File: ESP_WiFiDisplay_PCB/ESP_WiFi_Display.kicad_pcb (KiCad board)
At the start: 2 copper layers, 50 x 100 mm, 30 parts, among them CON1 BARREL_JACK, P1 SERIAL_HC12, P10 POWER, P2 USB, P3 NODEMCU_1, P4 NODEMCU_2, P5 LOCAL 5V?, P6 WS2812 LED, P7 PCB, P8 LOGO1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

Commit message: PCB changes
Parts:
- removed CON1: BARREL_JACK, REInnovationFootprint:DC_Power_2_1
- removed R2: 330, REInnovationFootprint:TH_Resistor_1
- removed R3, R4: 10k, REInnovationFootprint:TH_Resistor_1
- removed SW2: SWDOWN, REInnovationFootprint:SW_PUSH_SMALL_lg_pad
- removed SW3: ON/OFF, REInnovationFootprint:SW_SPDT_R_Angle_ALIEX
- removed U3: 74LVC1G17, REInnovationFootprint:SM_SOT-23-5
- added C3: 100n, matts_components:C1_wide_lg_pad, F.Cu at (112.4, 47.0)
- added C4: 100n, matts_components:C1_wide_lg_pad, F.Cu at (121.3, 47.0)
- added C5: 100n, matts_components:C1_wide_lg_pad, F.Cu at (130.2, 47.0)
- added D6: WS2812, LEDs:LED_WS2812B-PLCC4, F.Cu at (122.6, 41.9)
- added D7: WS2812, LEDs:LED_WS2812B-PLCC4, F.Cu at (131.4, 41.9)
- added ENC1: Encoder_1, matts_components:Encoder, F.Cu at (113.7, 112.4)
- C1, C2: value 10u -> 100n; footprint REInnovationFootprint:C_1V7_TH -> matts_components:C1_wide_lg_pad
- D1: value WS2811_EpiStar_8mm -> D_Schottky; footprint REInnovationFootprint:TH_WS2811_LED_8mm -> REInnovationFootprint:TH_Diode_1
- D2: value A -> B
- D3: value B -> WS2812; footprint REInnovationFootprint:TH_LED-5MM_larg_pad -> LEDs:LED_WS2812B-PLCC4
- D4, D5: value D_Schottky -> WS2812; footprint REInnovationFootprint:TH_Diode_1 -> LEDs:LED_WS2812B-PLCC4
- P1: value SERIAL_HC12 -> USB_Micro; footprint REInnovationFootprint:TH_SIL_5_1mm -> REInnovationFootprint:USB_Micro-B_MOLEX_47642-0001
- P10: value POWER -> 5V_EXT; footprint REInnovationFootprint:SIL-2_screw_terminal -> REInnovationFootprint:TH_CONN_2W
- P5: value LOCAL 5V? -> PCB; footprint matts_components:SIL-2_solder_connect -> REInnovationFootprint:PCB_50x100mm_RJWIFI
- P6: value WS2812 LED -> LOGO1; footprint matts_components:SIL-4_screw_terminals -> CuriousElectric3:CEC_Globe_10mm_FCU
- P7: value PCB -> LOGO2; footprint REInnovationFootprint:PCB_50x100mm_RJWIFI -> CuriousElectric3:TCEC_Words_13mm
- P8: value LOGO1 -> SERIAL_HC12; footprint CuriousElectric3:CEC_Globe_10mm_FCU -> REInnovationFootprint:TH_SIL_5_1mm
- P9: value LOGO2 -> S_SERIAL; footprint CuriousElectric3:TCEC_Words_13mm -> matts_components:SIL-4_screw_terminals
- SW1: value SWUP -> ON/OFF; footprint REInnovationFootprint:SW_PUSH_SMALL_lg_pad -> REInnovationFootprint:SW_SPDT_R_Angle_ALIEX
- U2: value L4940V5 -> 74LVC1G17; footprint REInnovationFootprint:TO220_7805_Vert -> REInnovationFootprint:SM_SOT-23-5
- moved P5 84.6 mm to (88.9, 137.2)
- moved C1 79.3 mm to (94.6, 47.0), turned to 0 degrees
- moved C2 79.1 mm to (103.5, 47.0), turned to 0 degrees
- moved D5 77.3 mm to (113.7, 41.9), turned to 0 degrees
- moved D4 76.2 mm to (104.8, 41.9)
- moved D1 73.7 mm to (104.8, 113.7), turned to 90 degrees
- moved U2 70.9 mm to (104.8, 61.6), turned to 270 degrees
- moved P1 68.5 mm to (139.1, 116.8), turned to 90 degrees
- moved SW1 65.9 mm to (92.7, 111.8), turned to 180 degrees
- moved D2 46.3 mm to (134.0, 72.4)
- moved P6 43.9 mm to (53.4, 41.9)
- moved D3 37.5 mm to (95.9, 41.9), turned to 0 degrees
- moved P7 37.2 mm to (56.6, 151.6)
- moved P8 35.6 mm to (111.1, 73.7), turned to 180 degrees
- moved P9 27.8 mm to (93.3, 59.1), turned to 270 degrees
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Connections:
- net /SW_DOWN renamed /ENC_A
- C1 pad 1: Net-(C1-Pad1) -> /5V_PWR
- C2 pad 1: Net-(C2-Pad1) -> /5V_PWR
- D1 pad 1: (no net) -> Net-(D1-Pad1)
- D1 pad 2: /5V_PWR -> Net-(D1-Pad2)
- D3 pad 1: GND -> Net-(D3-Pad1)
- D3 pad 2: Net-(D3-Pad2) -> /5V_PWR
- D4 pad 1: Net-(C1-Pad1) -> Net-(D4-Pad1)
- D4 pad 2: Net-(CON1-Pad1) -> /5V_PWR
- D5 pad 1: Net-(C2-Pad1) -> Net-(D5-Pad1)
- D5 pad 2: Net-(D5-Pad2) -> /5V_PWR
- F1 pad 1: Net-(C2-Pad1) -> Net-(D1-Pad1)
- P1 pad 1: /HC12_SET -> Net-(D1-Pad2)
- P1 pad 2: /SOFT_Rx -> (no net)
- P1 pad 3: /SOFT_Tx -> (no net)
- P1 pad 4: GND -> (no net)
- P1 pad 5: +3V3 -> GND
- P10 pad 1: Net-(CON1-Pad1) -> Net-(D1-Pad2)
- P2 pad 1: Net-(D5-Pad2) -> Net-(D1-Pad2)
- P4 pad 14: /HC12_SET -> /ENC_B
- P4 pad 15: /SW_UP -> /HC12_SET
- P4 pad 5: /LED_A -> /SW_ENC
- P6 pad 1: Net-(P5-Pad2) -> (no net)
- P8 pad 1: (no net) -> /HC12_SET
- R1 pad 1: /LED_A -> /LED_WS2811
- SW1 pad 1: /SW_UP -> Net-(F1-Pad2)
- SW1 pad 2: GND -> /5V_PWR
- U1 pad 20: /LED_A -> /SW_ENC
- U1 pad 29: /HC12_SET -> /ENC_B
- U1 pad 30: /SW_UP -> /HC12_SET
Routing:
- net GND: track 389.4 -> 0.06 mm
- net /5V_PWR: track 163.1 -> 0.06 mm, vias 1 -> 0
- net +3V3: track 121.0 -> 0.00 mm
- net /SW_UP: track 102.2 -> 0.00 mm
- net /ENC_A: track 76.1 -> 0.00 mm
- net /HC12_SET: track 71.0 -> 0.00 mm
- net /SOFT_Tx: track 69.9 -> 0.00 mm
- net /SOFT_Rx: track 69.7 -> 0.00 mm
- net Net-(D1-Pad4): track 65.1 -> 0.00 mm, vias 1 -> 0
- net /SDA: track 41.9 -> 0.00 mm
- net /SCL: track 36.5 -> 0.00 mm
- net Net-(F1-Pad2): track 35.3 -> 0.00 mm
- net Net-(D2-Pad2): track 32.7 -> 0.00 mm
- net /LED_A: track 25.7 -> 0.00 mm
- net /LED_WS2811: track 23.7 -> 0.00 mm
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- removed copper zone on B.Cu, net GND
- removed copper zone on F.Cu, net GND
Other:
- board text removed: "5-12VDC"

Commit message: Small PCB changes
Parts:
- removed P2: USB, REInnovationFootprint:TH_USB_B_lg_pad
- added D8: LED, REInnovationFootprint:TH_LED-5MM_larg_pad, F.Cu at (126.4, 112.4)
- D1: value D_Schottky -> 1N5819
- D2: value B -> 1N5819; footprint REInnovationFootprint:TH_LED-5MM_larg_pad -> REInnovationFootprint:TH_Diode_1
- ENC1: value Encoder_1 -> Encoder
- P8: footprint REInnovationFootprint:TH_SIL_5_1mm -> REInnovationFootprint:TH_SIL_5_HC12
- moved P7 117.5 mm to (142.9, 71.8)
- moved P6 82.5 mm to (132.7, 64.8), turned to 0 degrees
- moved D2 61.3 mm to (101.6, 124.5), turned to 90 degrees
- moved R1 26.2 mm to (122.6, 87.0)
- moved P10 13.4 mm to (116.8, 128.3)
- moved D1 10.8 mm to (104.8, 124.5)
- moved P8 8.03 mm to (113.7, 66.0), turned to 0 degrees
- moved U2 2.29 mm to (103.5, 59.7)
- moved F1 1.42 mm to (102.9, 114.9)
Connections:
- D2 pad 1: GND -> Net-(D1-Pad1)
- P10 pad 1: Net-(D1-Pad2) -> Net-(D2-Pad2)
- R1 pad 2: Net-(D2-Pad2) -> Net-(D8-Pad2)
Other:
- board text added: "+3.3"
- board text added: "GND"
- board text added: "Rx"
- board text added: "Tx"

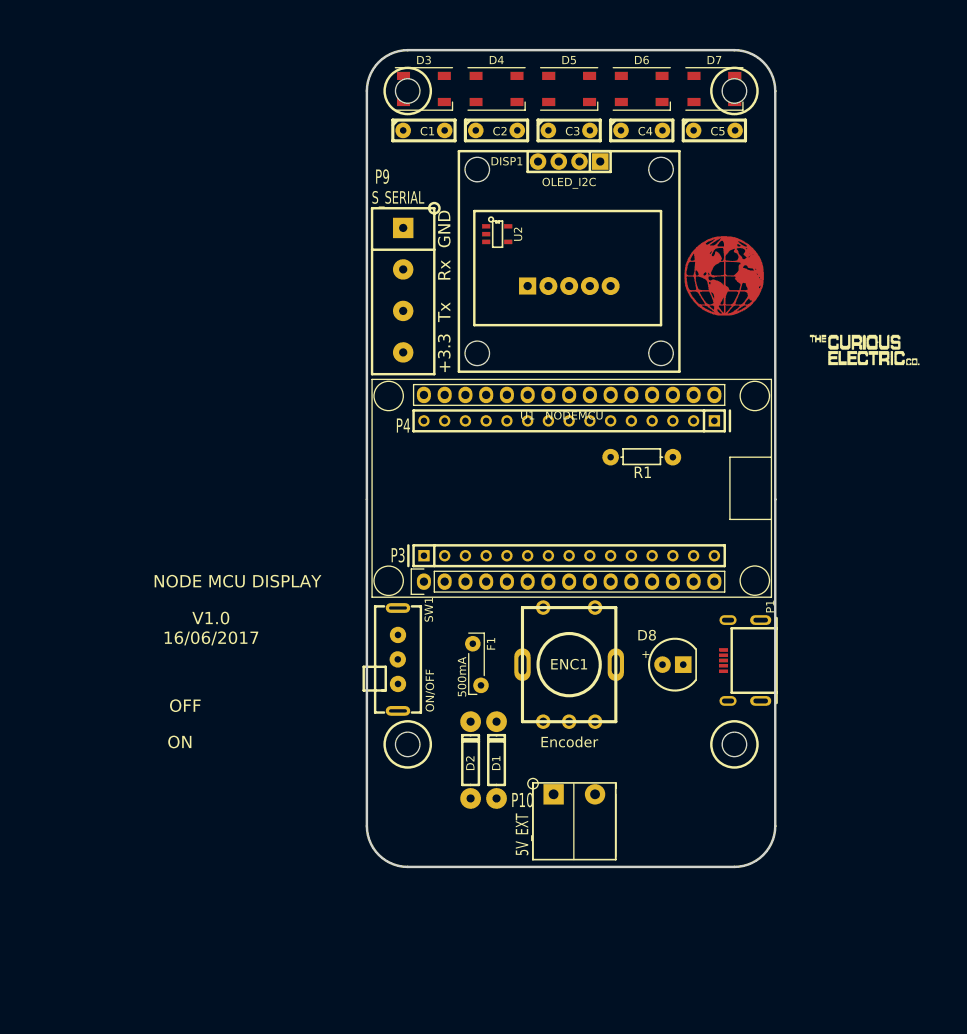
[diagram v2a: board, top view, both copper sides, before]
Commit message: PCB initial wiring. Cost and Parts info done
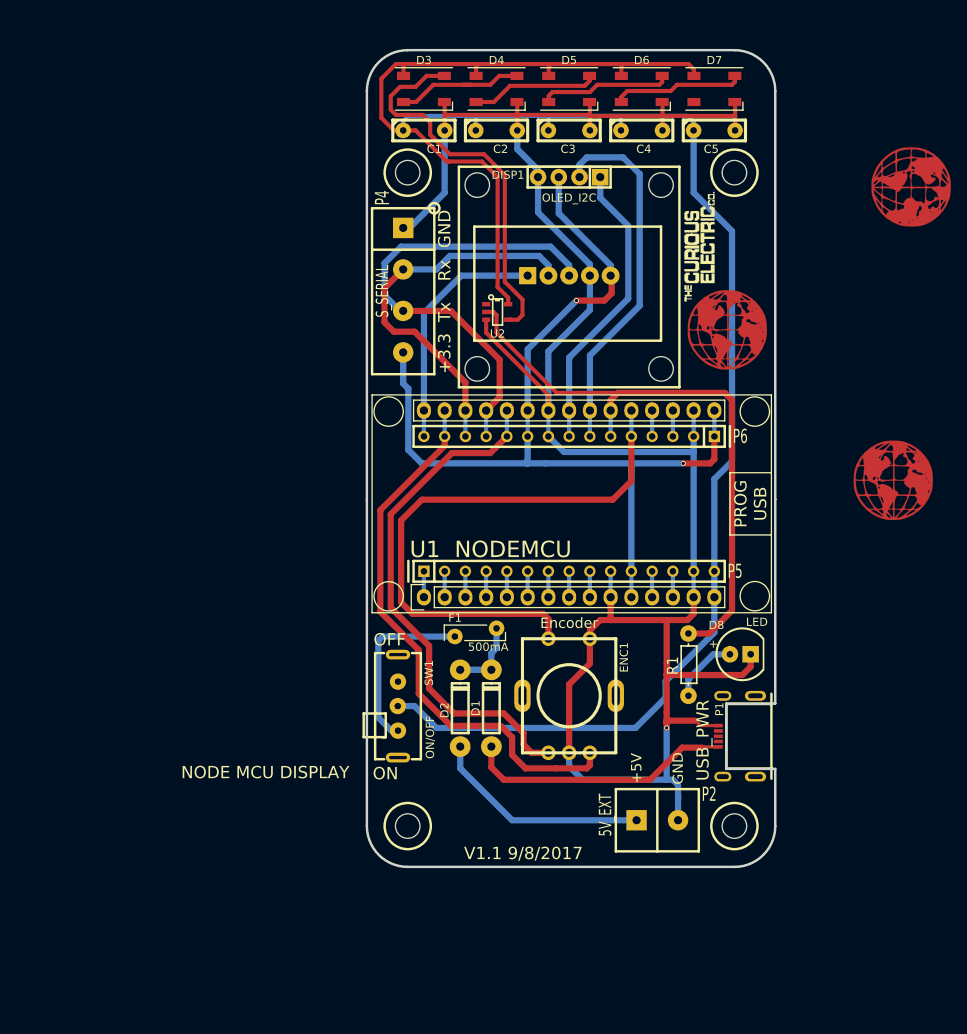
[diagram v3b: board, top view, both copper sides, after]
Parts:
- added P11: LOGO2, CuriousElectric3:TCEC_Words_13mm, F.Cu at (127.5, 68.2)
- added P2: 5V_EXT, matts_components:SIL-2_screw_terminal, F.Cu at (121.9, 131.4)
- D3, D4, D5, D6, D7: value WS2812 -> WS2812B_SMD; footprint LEDs:LED_WS2812B-PLCC4 -> REInnovationFootprint:SM_WS2812B
- ENC1: footprint matts_components:Encoder -> REInnovationFootprint:TH_Encoder
- P1: value USB_Micro -> USB_PWR
- P10: value 5V_EXT -> LOGO1; footprint REInnovationFootprint:TH_CONN_2W -> CuriousElectric3:CEC_Globe_10mm_FCU
- P3: value NODEMCU_1 -> SERIAL_HC12; footprint REInnovationFootprint:TH_SIL-15 -> REInnovationFootprint:TH_SIL_5_HC12
- P4: value NODEMCU_2 -> S_SERIAL; footprint REInnovationFootprint:TH_SIL-15 -> matts_components:SIL-4_screw_terminals
- P5: value PCB -> NODEMCU_1; footprint REInnovationFootprint:PCB_50x100mm_RJWIFI -> REInnovationFootprint:TH_SIL-15
- P6: value LOGO1 -> NODEMCU_2; footprint CuriousElectric3:CEC_Globe_10mm_FCU -> REInnovationFootprint:TH_SIL-15
- P7: value LOGO2 -> PCB; footprint CuriousElectric3:TCEC_Words_13mm -> REInnovationFootprint:PCB_50x100mm_RJWIFI
- P8: value SERIAL_HC12 -> LOGO_MOUSE; footprint REInnovationFootprint:TH_SIL_5_HC12 -> CuriousElectric3:CEC_Globe_10mm_FCU
- P9: value S_SERIAL -> HARDWARE; footprint matts_components:SIL-4_screw_terminals -> CuriousElectric3:CEC_Globe_10mm_FCU
- moved P7 84.8 mm to (88.9, 137.2)
- moved P9 62.4 mm to (155.6, 54.0)
- moved P10 59.2 mm to (133.1, 71.4)
- moved P8 46.3 mm to (153.4, 89.8)
- moved P5 40.6 mm to (107.3, 101.0)
- moved P4 35.5 mm to (93.3, 59.1), turned to 270 degrees
- moved P3 34.9 mm to (113.7, 64.8)
- moved R1 26.0 mm to (128.3, 112.4), turned to 270 degrees
- moved P6 23.4 mm to (120.0, 84.5), turned to 180 degrees
- moved U2 9.53 mm to (103.5, 69.2)
- moved P1 9.29 mm to (138.4, 126.1)
- moved D8 8.35 mm to (134.6, 111.1)
- moved F1 7.24 mm to (104.8, 108.0), turned to 180 degrees
- moved D2 6.48 mm to (100.3, 118.1)
- moved D1 6.38 mm to (104.1, 118.1)
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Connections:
- D3 pad 1: Net-(D3-Pad1) -> /5V_PWR
- D3 pad 2: /5V_PWR -> Net-(D3-Pad2)
- D4 pad 1: Net-(D4-Pad1) -> /5V_PWR
- D4 pad 2: /5V_PWR -> Net-(D4-Pad2)
- D4 pad 4: Net-(D3-Pad1) -> Net-(D3-Pad2)
- D5 pad 1: Net-(D5-Pad1) -> /5V_PWR
- D5 pad 2: /5V_PWR -> Net-(D5-Pad2)
- D5 pad 4: Net-(D4-Pad1) -> Net-(D4-Pad2)
- D6 pad 1: Net-(D6-Pad1) -> /5V_PWR
- D6 pad 2: /5V_PWR -> Net-(D6-Pad2)
- D6 pad 4: Net-(D5-Pad1) -> Net-(D5-Pad2)
- D7 pad 1: (no net) -> /5V_PWR
- D7 pad 2: /5V_PWR -> (no net)
- D7 pad 4: Net-(D6-Pad1) -> Net-(D6-Pad2)
- P10 pad 1: Net-(D2-Pad2) -> (no net)
- P3 pad 1: Net-(P3-Pad1) -> /HC12_SET
- P3 pad 2: Net-(P3-Pad2) -> /SOFT_Rx
- P3 pad 3: Net-(P3-Pad3) -> /SOFT_Tx
- P3 pad 4: Net-(P3-Pad4) -> GND
- P3 pad 5: Net-(P3-Pad5) -> +3V3
- P4 pad 1: +3V3 -> GND
- P4 pad 2: GND -> /SOFT_Rx
- P4 pad 3: /Tx -> /SOFT_Tx
- P4 pad 4: /Rx -> +3V3
- P6 pad 1: (no net) -> +3V3
- P8 pad 1: /HC12_SET -> (no net)
- P9 pad 1: GND -> (no net)
- U1 pad 1: Net-(P3-Pad1) -> Net-(P5-Pad1)
- U1 pad 12: Net-(P3-Pad12) -> Net-(P5-Pad12)
- U1 pad 13: Net-(P3-Pad13) -> Net-(P5-Pad13)
- U1 pad 2: Net-(P3-Pad2) -> Net-(P5-Pad2)
- U1 pad 3: Net-(P3-Pad3) -> Net-(P5-Pad3)
- U1 pad 4: Net-(P3-Pad4) -> Net-(P5-Pad4)
- U1 pad 5: Net-(P3-Pad5) -> Net-(P5-Pad5)
- U1 pad 6: Net-(P3-Pad6) -> Net-(P5-Pad6)
- U1 pad 7: Net-(P3-Pad7) -> Net-(P5-Pad7)
- U1 pad 8: Net-(P3-Pad8) -> Net-(P5-Pad8)
- U1 pad 9: Net-(P3-Pad9) -> Net-(P5-Pad9)
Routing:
- net GND: track 0.06 -> 267.1 mm, vias 0 -> 1
- net /5V_PWR: track 0.06 -> 239.8 mm
- net +3V3: track 0.00 -> 117.7 mm, vias 0 -> 2
- net /LED_WS2811: track 0.00 -> 73.8 mm
- net /SW_ENC: track 0.00 -> 70.2 mm
- net /ENC_B: track 0.00 -> 67.6 mm
- net /ENC_A: track 0.00 -> 63.3 mm
- net /SOFT_Tx: track 0.00 -> 57.0 mm
- net Net-(D3-Pad4): track 0.00 -> 47.4 mm
- net /SOFT_Rx: track 0.00 -> 47.2 mm
- net /SCL: track 0.00 -> 44.8 mm
- net /SDA: track 0.00 -> 36.2 mm
- net Net-(D1-Pad2): track 0.00 -> 32.6 mm
- net /HC12_SET: track 0.00 -> 29.7 mm
- net Net-(D2-Pad2): track 0.00 -> 26.9 mm
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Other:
- outline, holes or cut-outs redrawn
- net class Default: trace_width 0.762 -> 0.508
- board text added: "3.3V"
- board text added: "A0"
- board text added: "D0"
- board text added: "D1"
- board text added: "D2"
- board text added: "D3"
- board text added: "D4"
- board text added: "D5"
- board text added: "D6"
- board text added: "D7"
- board text added: "D8"
- board text added: "PROG USB"
- board text added: "V1.1 9/8/2017"
- board text added: "Vin"
- board text removed: "V1.0 16/06/2017"

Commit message: Full review of boards - needs NAME still!
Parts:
- removed P9: HARDWARE, CuriousElectric3:CEC_Globe_10mm_FCU
- P1: value USB_PWR -> USB_Micro
- P8: footprint CuriousElectric3:CEC_Globe_10mm_FCU -> CuriousElectric3:mouse10x10
- moved P8 26.5 mm to (133.0, 72.9)
- moved P10 11.4 mm to (128.0, 61.2)
- moved P11 5.91 mm to (133.3, 67.3)
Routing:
- net +3V3: track 117.7 -> 131.1 mm
- net /SW_ENC: track 70.2 -> 73.7 mm

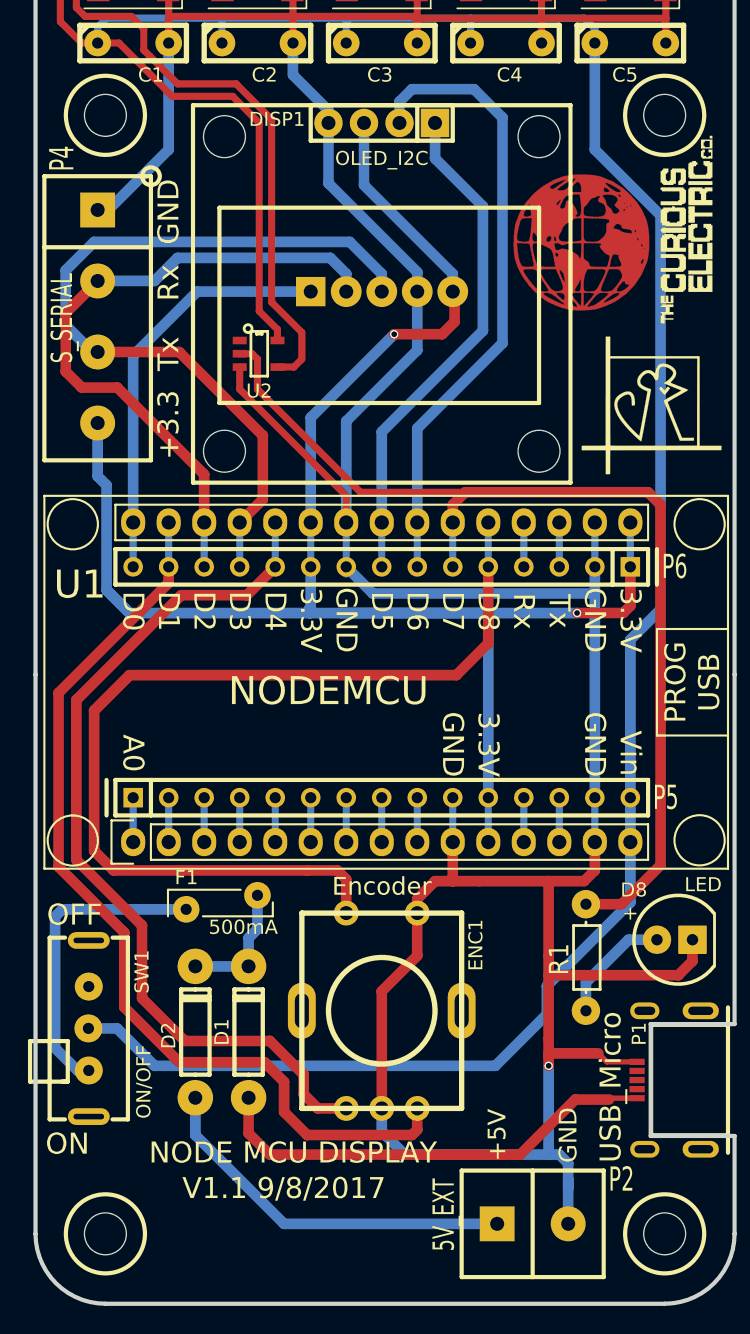
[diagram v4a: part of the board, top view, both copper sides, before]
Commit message: Updated PCB with name
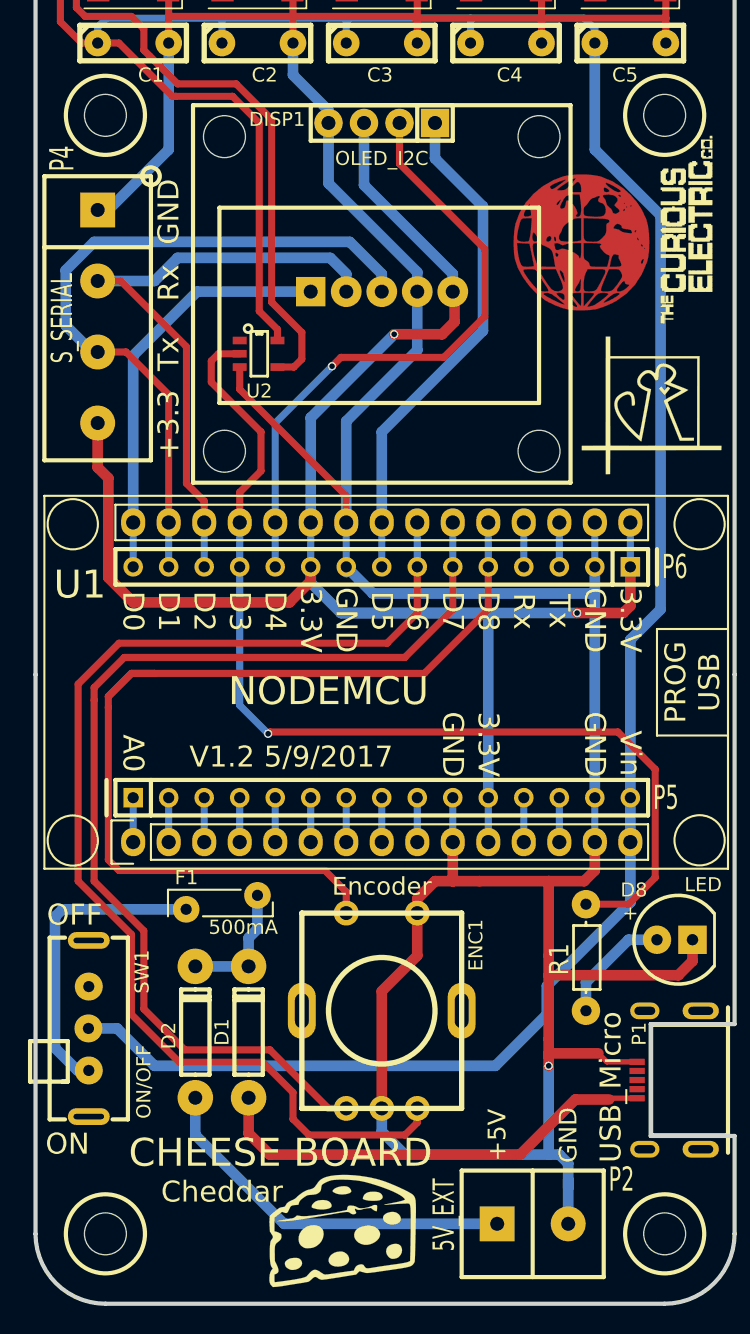
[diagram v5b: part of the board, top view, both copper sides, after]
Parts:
- added P13: LOGO_CHEESE, CuriousElectric3:CheeseWedge8mm, F.Cu at (110.9, 132.0)
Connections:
- P6 pad 11: /ENC_A -> /SCL
- P6 pad 12: /SOFT_Tx -> /LED_WS2811
- P6 pad 14: /ENC_B -> /SOFT_Tx
- P6 pad 6: /LED_WS2811 -> /ENC_A
- P6 pad 7: /SCL -> /ENC_B
- U1 pad 21: /LED_WS2811 -> /ENC_A
- U1 pad 22: /SCL -> /ENC_B
- U1 pad 26: /ENC_A -> /SCL
- U1 pad 27: /SOFT_Tx -> /LED_WS2811
- U1 pad 29: /ENC_B -> /SOFT_Tx
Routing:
- net /ENC_B: track 67.6 -> 84.6 mm
- net /ENC_A: track 63.3 -> 76.1 mm
- net /SOFT_Tx: track 57.0 -> 51.3 mm
- net +3V3: track 131.1 -> 127.1 mm
- net /SW_ENC: track 73.7 -> 71.1 mm
- net /SOFT_Rx: track 47.2 -> 44.8 mm
- net /LED_WS2811: track 73.8 -> 74.2 mm, vias 0 -> 1
- net /SCL: vias 0 -> 1
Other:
- net class Default: trace_width 0.508 -> 0.762
- board text added: "CHEESE BOARD"
- board text added: "Cheddar"
- board text added: "V1.2 5/9/2017"
- board text removed: "NODE MCU DISPLAY"
- board text removed: "V1.1 9/8/2017"
